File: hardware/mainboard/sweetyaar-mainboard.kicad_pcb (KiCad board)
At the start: 4 copper layers, 80 x 80 mm, 104 parts, among them Q1 MMBT3904

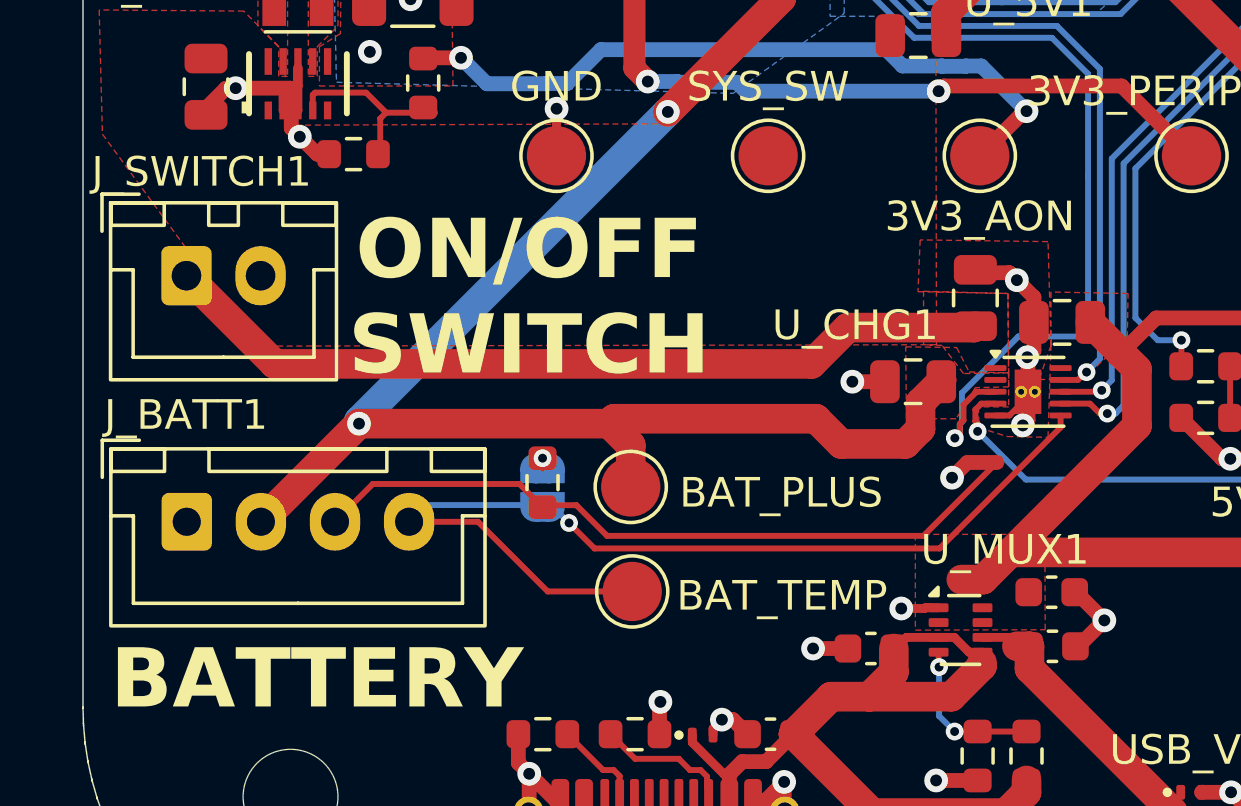
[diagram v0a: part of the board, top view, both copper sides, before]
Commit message: changing battery connector to 5 pins (one unused) for better protection against assembly mistakes
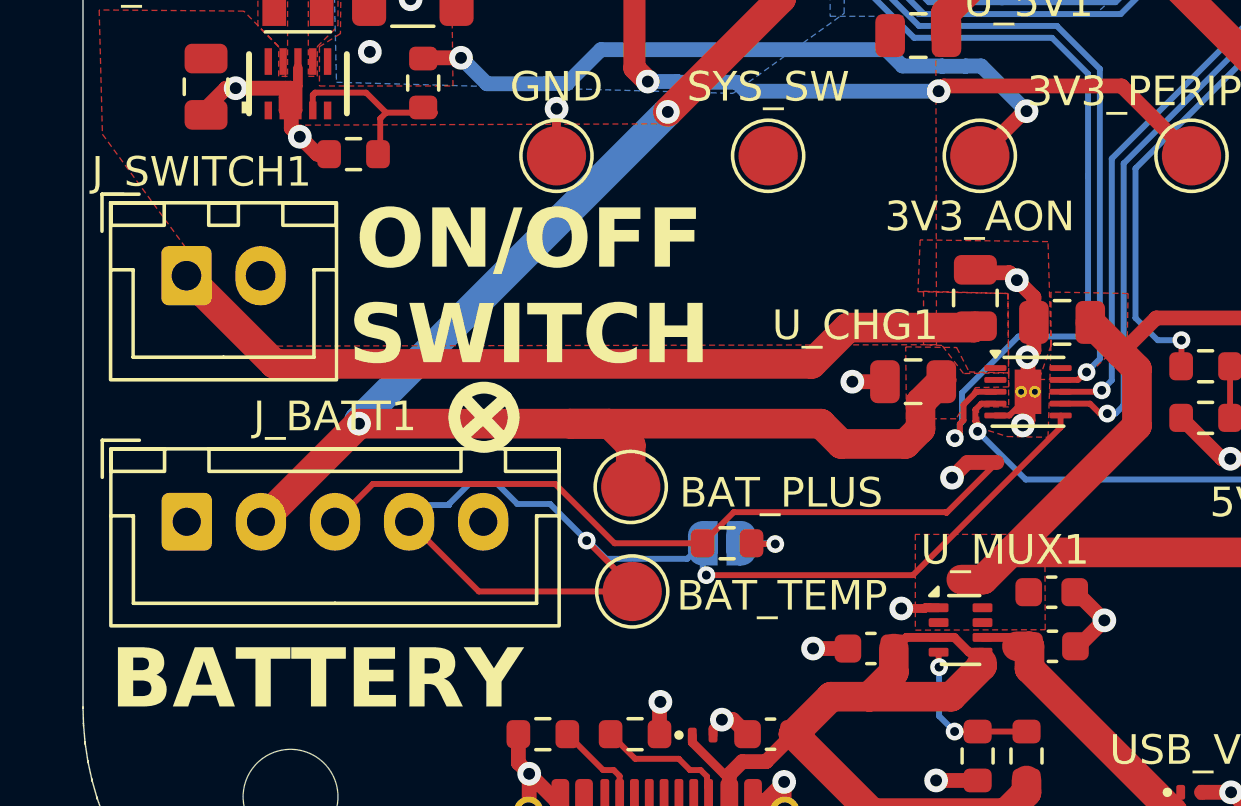
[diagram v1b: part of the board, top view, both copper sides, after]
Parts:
- J_BATT1: footprint Connector_JST:JST_XH_B4B-XH-A_1x04_P2.50mm_Vertical -> Connector_JST:JST_XH_B5B-XH-A_1x05_P2.50mm_Vertical
- moved R_TH1 6.55 mm to (41.7, 84.5), turned to 180 degrees
- moved JP3 6.34 mm to (41.6, 84.5), turned to 180 degrees
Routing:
- net BAT_TEMP: track 33.5 -> 38.1 mm, vias 1 -> 2
- net Net-(JP3-A): track 0.34 -> 1.97 mm
- net BAT_PLUS: track 87.3 -> 88.5 mm

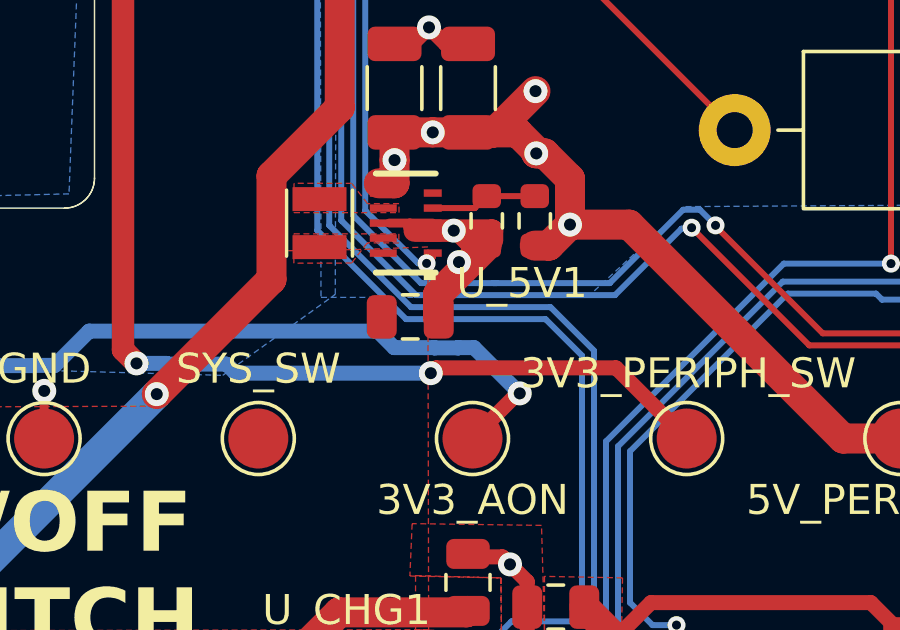
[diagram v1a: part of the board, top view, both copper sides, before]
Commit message: Adding a solder jumper (open) to allow changing 5V regulator MODE to PWM.
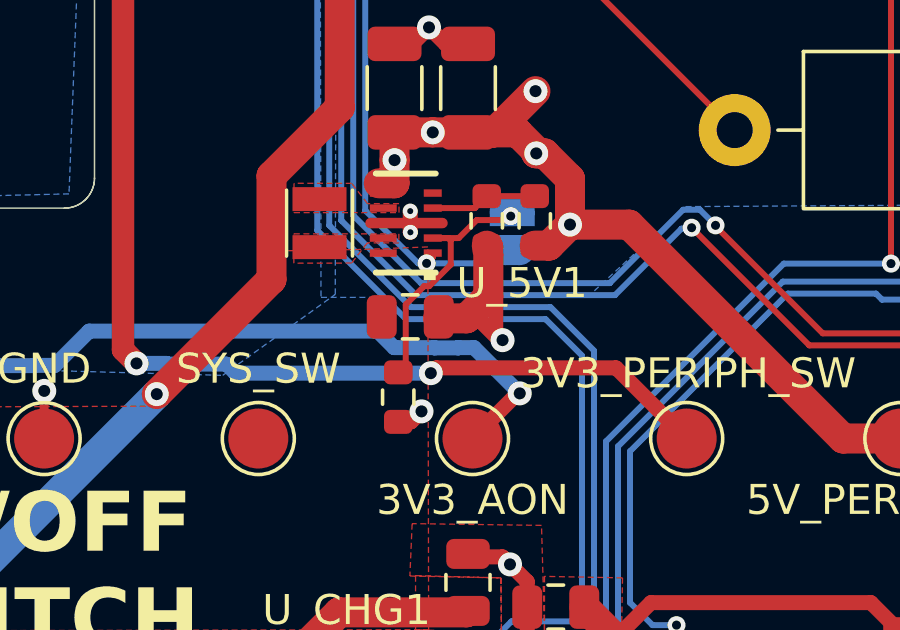
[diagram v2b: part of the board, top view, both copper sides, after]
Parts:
- added JP4: SolderJumper_2_Open, Jumper:SolderJumper-2_P1.3mm_Open_RoundedPad1.0x1.5mm, B.Cu at (51.6, 64.5)
- added R_MODE_PD1: 100k, Resistor_SMD:R_0603_1608Metric, F.Cu at (47.8, 70.0)
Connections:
- U_5V1 pad 2: GND -> Net-(JP4-B)
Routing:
- net Net-(JP4-B): track 0.00 -> 8.88 mm, vias 0 -> 1
- net GND: track 134.9 -> 139.2 mm, vias 54 -> 56
- net /PERIPH_PWR_EN: track 59.9 -> 62.9 mm
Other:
- board text added: "Bridge to force 5V regulator PWM mode."

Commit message: Adding more thermal vias on amp and charger ICs
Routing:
- net GND: track 139.2 -> 146.4 mm, vias 56 -> 63
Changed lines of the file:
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@@
+	)
+	(segment
+		(start 51.875 78.52)
+		(end 51.875 78.2)
+		(width 0.5)
+		(layer "F.Cu")
+		(net "GND")
 	)
 	(segment
@@
 	)
 	(segment
+		(start 27.025 69.251805)
+		(end 27.025512 69.252317)
+		(width 0.5)
+		(layer "F.Cu")
+		(net "GND")
+	)
+	(segment
 		(start 89.233972 41.5425)
 		(end 89.476472 41.3)
@@
 	)
 	(segment
-		(start 48.25 58.225)
-		(end 48.8 57.675)
-		(width 0.5)
-		(layer "F.Cu")
-		(net "GND")
-	)
-	(segment
 		(start 39.125 40.75)
 		(end 39.125 40.625)
@@
 		(start 35.05 92.225)
 		(end 35.05 94.02)
+		(width 0.5)
+		(layer "F.Cu")
+		(net "GND")
+	)
+	(segment
+		(start 49.35 58.225)
+		(end 50.10091 58.225)
+		(width 0.5)
+		(layer "F.Cu")
+		(net "GND")
+	)
+	(segment
+		(start 47.65091 58.225)
+		(end 50.10091 58.225)
 		(width 0.5)
 		(layer "F.Cu")
@@
 	)
 	(segment
+		(start 48.8 57.675)
+		(end 48.25 58.225)
+		(width 0.5)
+		(layer "F.Cu")
+		(net "GND")
+	)
+	(segment
 		(start 50.05 67.375)
 		(end 49.175 67.375)
@@
 	)
 	(segment
-		(start 49.35 58.225)
-		(end 48.8 57.675)
-		(width 0.5)
-		(layer "F.Cu")
-		(net "GND")
-	)
-	(segment
 		(start 44.0125 35.7875)
 		(end 43.925 35.7)
@@
 	)
 	(segment
+		(start 50.10091 58.225)
+		(end 49.625 58.225)
+		(width 0.5)
+		(layer "F.Cu")
+		(net "GND")
+	)
+	(segment
+		(start 48.8 57.4)
+		(end 48.8 57.675)
+		(width 0.5)
+		(layer "F.Cu")
+		(net "GND")
+	)
+	(segment
 		(start 35.97 71.38)
 		(end 35.97 69.797032)
@@
 	)
 	(segment
-		(start 47.65091 58.225)
-		(end 48.25 58.225)
-		(width 0.5)
-		(layer "F.Cu")
-		(net "GND")
-	)
-	(segment
 		(start 57.04 80.22)
 		(end 58.42 81.6)
@@
 		(start 67.125 85.375)
 		(end 65.1 85.375)
+		(width 0.5)
+		(layer "F.Cu")
+		(net "GND")
+	)
+	(segment
+		(start 48.8 57.675)
+		(end 49.35 58.225)
 		(width 0.5)
 		(layer "F.Cu")
@@
 	)
 	(segment
+		(start 48.8 57.4)
+		(end 48.8 58.85)
+		(width 0.5)
+		(layer "F.Cu")
+		(net "GND")
+	)
+	(segment
+		(start 48.25 58.225)
+		(end 47.65091 58.225)
+		(width 0.5)
+		(layer "F.Cu")
+		(net "GND")
+	)
+	(segment
 		(start 34.685 90.89)
 		(end 34.685 91.86)
@@
 		(start 56.95 47.7)
 		(end 56.975 47.725)
+		(width 0.5)
+		(layer "F.Cu")
+		(net "GND")
+	)
+	(segment
+		(start 47.65091 58.225)
+		(end 48.175 58.225)
 		(width 0.5)
 		(layer "F.Cu")
@@
 	)
 	(segment
+		(start 48.175 58.225)
+		(end 48.9 58.95)
+		(width 0.5)
+		(layer "F.Cu")
+		(net "GND")
+	)
+	(segment
 		(start 47.625 32.975)
 		(end 49.025 32.975)
@@
 	(segment
 		(start 51.875 79.34)
-		(end 51.875 78.2)
+		(end 51.875 78.52)
+		(width 0.5)
+		(layer "F.Cu")
+		(net "GND")
+	)
+	(segment
+		(start 49.625 58.225)
+		(end 48.9 58.95)
 		(width 0.5)
 		(layer "F.Cu")
@@
 	)
 	(segment
+		(start 48.8 58.85)
+		(end 48.9 58.95)
+		(width 0.5)
+		(layer "F.Cu")
+		(net "GND")
+	)
+	(segment
 		(start 88.75 50.24)
 		(end 88.96 50.24)
@@
 	)
 	(segment
+		(start 27.025 69.124999)
+		(end 27.025 69.251805)
+		(width 0.5)
+		(layer "F.Cu")
+		(net "GND")
+	)
+	(segment
 		(start 51.875 79.34)
 		(end 51.875 80.3)
@@
 	)
 	(segment
-		(start 51.875 80.3)
-		(end 51.7 80.475)
-		(width 0.5)
-		(layer "F.Cu")
-		(net "GND")
-	)
-	(segment
 		(start 38.8 43.225)
 		(end 38.775 43.2)
@@
 		(start 42.8125 35.7875)
 		(end 41.7625 35.7875)
-		(width 0.5)
-		(layer "F.Cu")
-		(net "GND")
-	)
-	(segment
-		(start 50.10091 58.225)
-		(end 49.35 58.225)
 		(width 0.5)
 		(layer "F.Cu")
@@
 	)
 	(via
-		(at 48.8 57.675)
+		(at 48.8 57.4)
 		(size 0.8)
 		(drill 0.4)
@@
 	)
 	(via
-		(at 51.85 78.175)
+		(at 51.88 78.255)
 		(size 0.8)
 		(drill 0.4)
@@
 	)
 	(via
-		(at 51.7 80.475)
+		(at 52.034847 80.45)
 		(size 0.8)
 		(drill 0.4)
@@
 	)
 	(via
+		(at 86.69 41.79)
+		(size 0.5)
+		(drill 0.2)
+		(layers "F.Cu" "B.Cu")
+		(net "GND")
+	)
+	(via
 		(at 70.45 27.675)
 		(size 0.8)
@@
 	)
 	(via
+		(at 48.9 58.95)
+		(size 0.8)
+		(drill 0.4)
+		(layers "F.Cu" "B.Cu")
+		(net "GND")
+	)
+	(via
 		(at 48.55 70.475)
 		(size 0.8)
@@
 	)
 	(via
+		(at 87.2 41.2525)
+		(size 0.5)
+		(drill 0.2)
+		(layers "F.Cu" "B.Cu")
+		(net "GND")
+	)
+	(via
+		(at 87.7 41.8)
+		(size 0.5)
+		(drill 0.2)
+		(layers "F.Cu" "B.Cu")
+		(net "GND")
+	)
+	(via
 		(at 48.475 26.9)
 		(size 0.8)
@@
 	)
 	(via
+		(at 87.2 42.309999)
+		(size 0.5)
+		(drill 0.2)
+		(layers "F.Cu" "B.Cu")
+		(net "GND")
+	)
+	(via
+		(at 51.043779 80.44)
+		(size 0.8)
+		(drill 0.4)
+		(layers "F.Cu" "B.Cu")
+		(net "GND")
+	)
+	(via
 		(at 86.775 39.338792)
 		(size 0.8)
@@
 		(layers "F.Cu" "B.Cu")
 		(net "GND")
+	)
+	(via
+		(at 27.025512 69.252317)
+		(size 0.5)
+		(drill 0.2)
+		(layers "F.Cu" "B.Cu")
+		(net "GND")

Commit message: adding diodes protection for the ~long cables from the buttons, also adding series resistors
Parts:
- added D3: ESD441, SweetYaar:Texas_DPY0002A_0.6x1mm_P0.65mm, F.Cu at (75.5, 92.7)
- added D5: ESD441, SweetYaar:Texas_DPY0002A_0.6x1mm_P0.65mm, F.Cu at (80.0, 92.7)
- added R_BTN_ANIMAL1: 330, Resistor_SMD:R_0603_1608Metric, F.Cu at (71.6, 84.5)
- added R_BTN_SONG1: 330, Resistor_SMD:R_0603_1608Metric, F.Cu at (69.9, 84.5)
- moved LOGO 0.50 mm to (80.8, 79.5)
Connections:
- J_BTN1 pad 1: /BTN_SONG -> Net-(D3-K)
- J_BTN1 pad 3: /BTN_ANIMAL -> Net-(D5-K)
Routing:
- net /BTN_ANIMAL: track 92.8 -> 74.4 mm
- net Net-(D5-K): track 0.00 -> 16.5 mm
- net /BTN_SONG: track 88.8 -> 74.8 mm
- net Net-(D3-K): track 0.00 -> 13.3 mm
- net GND: track 146.4 -> 147.8 mm, vias 63 -> 65
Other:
- board text added: "ANIMALS"
- board text added: "SONGS"

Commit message: Adding a pull-down on LED DIN pin
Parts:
- added R_LED_DIN2: 100k, Resistor_SMD:R_0603_1608Metric, F.Cu at (94.9, 87.1)
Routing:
- net GND: track 147.8 -> 150.4 mm
- net Net-(D_LED1-DIN): track 53.8 -> 56.3 mm
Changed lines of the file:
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@@
 		)
 	)
+	(footprint "Resistor_SMD:R_0603_1608Metric"
+		(layer "F.Cu")
+		(at 94.87 87.08)
+		(descr "Resistor SMD 0603 (1608 Metric), square (rectangular) end terminal, IPC-7351 nominal, (Body size source: IPC-SM-782 page 72, https://www.pcb-3d.com/wordpress/wp-content/uploads/ipc-sm-782a_amendment_1_and_2.pdf)")
+		(tags "resistor")
+		(property "Reference" "R_LED_DIN2"
+			(at 0 -1.43 0)
+			(layer "F.SilkS")
+			(hide yes)
+			(effects
+				(font
+					(size 1 1)
+					(thickness 0.15)
+				)
+			)
+		)
+		(property "Value" "100k"
+			(at 0 1.43 0)
+			(layer "F.Fab")
+			(effects
+				(font
+					(size 1 1)
+					(thickness 0.15)
+				)
+			)
+		)
+		(property "Datasheet" ""
+			(at 0 0 0)
+			(layer "F.Fab")
+			(hide yes)
+			(effects
+				(font
+					(size 1.27 1.27)
+				)
+			)
+		)
+		(property "Description" ""
+			(at 0 0 0)
+			(layer "F.Fab")
+			(hide yes)
+			(effects
+				(font
+					(size 1.27 1.27)
+				)
+			)
+		)
+		(property "KiLib_Generator" "SMD_2terminal_chip_molded"
+			(at 0 0 0)
+			(layer "F.SilkS")
+			(hide yes)
+			(effects
+				(font
+					(size 1 1)
+					(thickness 0.15)
+				)
+			)
+		)
+		(property "LCSC" "C25803"
+			(at 0 0 0)
+			(unlocked yes)
+			(layer "F.Fab")
+			(hide yes)
+			(effects
+				(font
+					(size 1 1)
+					(thickness 0.15)
+				)
+			)
+		)
+		(property "FT Rotation Offset" ""
+			(at 0 0 0)
+			(unlocked yes)
+			(layer "F.Fab")
+			(hide yes)
+			(effects
+				(font
+					(size 1 1)
+					(thickness 0.15)
+				)
+			)
+		)
+		(property "Sim.Device" ""
+			(at 0 0 0)
+			(unlocked yes)
+			(layer "F.Fab")
+			(hide yes)
+			(effects
+				(font
+					(size 1 1)
+					(thickness 0.15)
+				)
+			)
+		)
+		(property "Sim.Pins" ""
+			(at 0 0 0)
+			(unlocked yes)
+			(layer "F.Fab")
+			(hide yes)
+			(effects
+				(font
+					(size 1 1)
+					(thickness 0.15)
+				)
+			)
+		)
+		(property ki_fp_filters "R_*")
+		(sheetname "/")
+		(sheetfile "sweetyaar-mainboard.kicad_sch")
+		(units
+			(unit
+				(name "A")
+				(pins "1" "2")
+			)
+		)
+		(attr smd)
+		(duplicate_pad_numbers_are_jumpers no)
+		(fp_line
+			(start -0.237258 -0.5225)
+			(end 0.237258 -0.5225)
+			(stroke
+				(width 0.12)
+				(type solid)
+			)
+			(layer "F.SilkS")
+		)
+		(fp_line
+			(start -0.237258 0.5225)
+			(end 0.237258 0.5225)
+			(stroke
+				(width 0.12)
+				(type solid)
+			)
+			(layer "F.SilkS")
+		)
+		(fp_rect
+			(start -1.48 -0.73)
+			(end 1.48 0.73)
+			(stroke
+				(width 0.05)
+				(type solid)
+			)
+			(fill no)
+			(layer "F.CrtYd")
+		)
+		(fp_rect
+			(start -0.8 -0.4125)
+			(end 0.8 0.4125)
+			(stroke
+				(width 0.1)
+				(type solid)
+			)
+			(fill no)
+			(layer "F.Fab")
+		)
+		(fp_text user "${REFERENCE}"
+			(at 0 0 0)
+			(layer "F.Fab")
+			(effects
+				(font
+					(size 0.4 0.4)
+					(thickness 0.06)
+				)
+			)
+		)
+		(pad "1" smd roundrect
+			(at -0.825 0)
+			(size 0.8 0.95)
+			(layers "F.Cu" "F.Mask" "F.Paste")
+			(roundrect_rratio 0.25)
+			(net "GND")
+			(pintype "passive")
+		)
+		(pad "2" smd roundrect
+			(at 0.825 0)
+			(size 0.8 0.95)
+			(layers "F.Cu" "F.Mask" "F.Paste")
+			(roundrect_rratio 0.25)
+			(net "Net-(D_LED1-DIN)")
+			(pintype "passive")
+		)
+		(embedded_fonts no)
+		(model "${KICAD10_3DMODEL_DIR}/Resistor_SMD.3dshapes/R_0603_1608Metric.step"
+			(offset
+				(xyz 0 0 0)
+			)
+			(scale
+				(xyz 1 1 1)
+			)
+			(rotate
+				(xyz 0 0 0)
+			)
+		)
+	)
 	(footprint "Capacitor_SMD:C_0805_2012Metric"
 		(layer "F.Cu")
@@
 	)
 	(segment
+		(start 94.045 85.695)
+		(end 93.175 84.825)
+		(width 0.5)
+		(layer "F.Cu")
+		(net "GND")
+	)
+	(segment
 		(start 95.76 64.18)
 		(end 94.08 64.18)
@@
 	)
 	(segment
+		(start 94.045 87.08)
+		(end 94.045 85.695)
+		(width 0.5)
+		(layer "F.Cu")
+		(net "GND")
+	)
+	(segment
 		(start 48.175001 63.90012)
 		(end 48.2 63.925119)
@@
 	)
 	(segment
+		(start 95.695 85.505)
+		(end 96.375 84.825)
+		(width 0.2)
+		(layer "F.Cu")
+		(net "Net-(D_LED1-DIN)")
+	)
+	(segment
 		(start 65.65 48.225)
 		(end 65.65 49.275)
@@
 		(width 0.2)
 		(layer "F.Cu")
+		(net "Net-(D_LED1-DIN)")
+	)
+	(segment
+		(start 95.695 87.08)
+		(end 95.695 85.505)
+		(width 0.2)
+		(layer "F.Cu")

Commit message: Changing power mux to TPS2121 (higher allowed voltage to deal with spikes and uncontrolled AUX)
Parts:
- removed R_CHARGER_CE_PU1: 100k, Resistor_SMD:R_0603_1608Metric
- added C_MUX_SS1: 100nF, 50 V, X7R, ±10%, Capacitor_SMD:C_0603_1608Metric, F.Cu at (55.7, 88.4)
- added R_CHARGER_CE_DIV1: 100k, Resistor_SMD:R_0603_1608Metric, F.Cu at (64.4, 76.4)
- added R_CHARGER_CE_DIV2: 91k, Resistor_SMD:R_0603_1608Metric, F.Cu at (64.4, 78.0)
- added R_MUX_ILIM1: 100k, Resistor_SMD:R_0603_1608Metric, F.Cu at (55.7, 91.6)
- added R_MUX_ILIM2: 100k, Resistor_SMD:R_0603_1608Metric, F.Cu at (55.7, 90.0)
- added R_MUX_OV_DIV1: 470k, Resistor_SMD:R_0603_1608Metric, F.Cu at (46.9, 88.9)
- added R_MUX_OV_DIV2: 100k, Resistor_SMD:R_0603_1608Metric, F.Cu at (48.5, 88.9)
- added R_MUX_OV_DIV3: 470k, Resistor_SMD:R_0603_1608Metric, F.Cu at (48.5, 85.8)
- added R_MUX_OV_DIV4: 100k, Resistor_SMD:R_0603_1608Metric, F.Cu at (46.9, 85.8)
- U_MUX1: value TPS2116DRLR -> TPS2121RUXR; footprint SweetYaar:SOT-583-8 - C3235557 -> Package_DFN_QFN:Texas_VQFN-HR-12_2x2.5mm_P0.5mm
- moved C_MUX1 6.64 mm to (52.4, 91.2), turned to 0 degrees
- moved R_PR1_TOP1 5.30 mm to (46.6, 92.4), turned to 180 degrees
- moved R_PR1_BOT1 4.28 mm to (46.6, 94.0), turned to 180 degrees
- moved U_MUX1 3.17 mm to (52.4, 88.9), turned to -90 degrees
- moved C_MUX2 2.23 mm to (50.9, 86.6), turned to 180 degrees
- moved C_MUX4 1.39 mm to (54.0, 86.6)
- moved NT1 1.07 mm to (49.3, 81.6)
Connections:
- U_MUX1 pad 1: GND -> /5V_INPUT
- U_MUX1 pad 2: /5V_INPUT -> AUX_5V_IN
- U_MUX1 pad 3: USB_VBUS -> GND
- U_MUX1 pad 4: /PR1 -> /MUX_OV2
- U_MUX1 pad 5: USB_VBUS -> /MUX_OV1
- U_MUX1 pad 6: AUX_5V_IN -> /PR1
- U_MUX1 pad 7: /5V_INPUT -> USB_VBUS
- U_MUX1 pad 8: unconnected-(U_MUX1-ST-Pad8) -> /5V_INPUT
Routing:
- net USB_VBUS: track 55.1 -> 37.5 mm
- net GND: track 150.4 -> 161.8 mm, vias 65 -> 71
- net /MUX_OV2: track 0.00 -> 5.20 mm
- net /MUX_OV1: track 0.00 -> 4.73 mm
- net AUX_5V_IN: track 26.5 -> 31.2 mm, vias 1 -> 3
- net /PR1: track 5.32 -> 9.26 mm
- net /MUX_ILIM: track 0.00 -> 3.31 mm
- net /5V_INPUT: track 32.2 -> 29.1 mm
- net /CHARGER_CE_N: track 18.0 -> 20.3 mm
- net /MUX_SS: track 0.00 -> 1.49 mm
- net /TS_RETURN: track 24.8 -> 23.8 mm
- added copper zone on F.Cu, net AUX_5V_IN
- added copper zone on F.Cu, net USB_VBUS
